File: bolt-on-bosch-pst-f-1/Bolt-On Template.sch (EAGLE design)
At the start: 10 parts

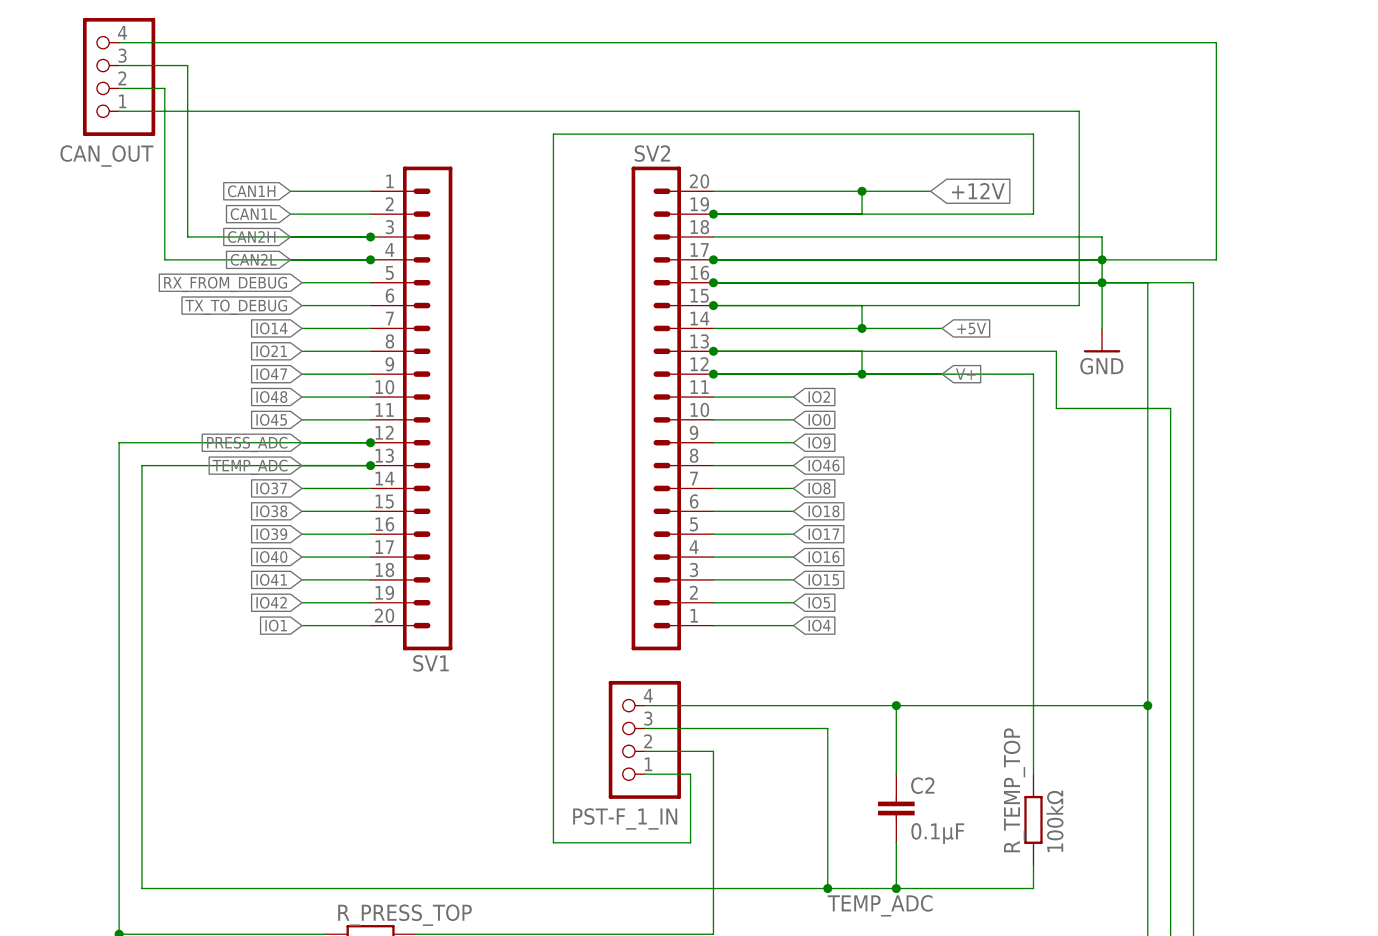
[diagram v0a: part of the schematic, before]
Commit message: designed circuit board for bosch sensor
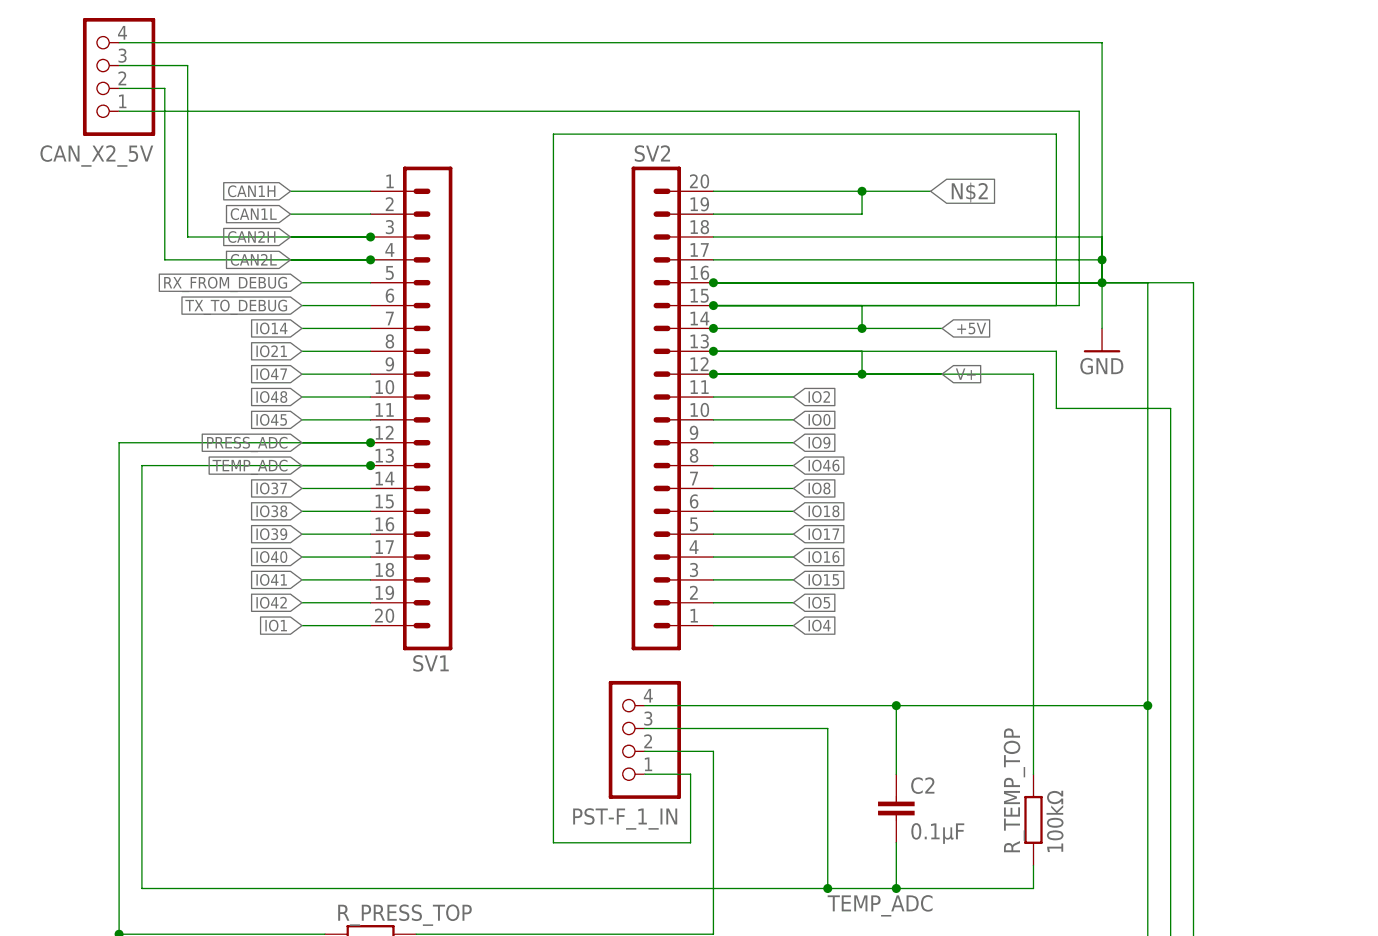
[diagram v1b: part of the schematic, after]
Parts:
- removed CAN_OUT: (no value), JST PH Library:S4B-PH-SM4-TB
- added CAN_X2_5V: (no value), JST PH Library:S4B-PH-K-S
- PST-F_1_IN: device JST PH Library:S4B-PH-SM4-TB -> JST PH Library:S4B-PH-K-S
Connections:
- removed net +12V: PST-F_1_IN.1, SV2.19, SV2.20
- new net N$2: SV2.19, SV2.20
- net +5V: now also CAN_X2_5V.1, PST-F_1_IN.1; no longer CAN_OUT.1
- net CAN2H: now also CAN_X2_5V.3; no longer CAN_OUT.3
- net CAN2L: now also CAN_X2_5V.2; no longer CAN_OUT.2
- net GND: now also CAN_X2_5V.4; no longer CAN_OUT.4
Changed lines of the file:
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@@
 <part name="R_PRESS_BOT" library="rcl" library_urn="urn:adsk.eagle:library:334" deviceset="R-EU_" device="R0805" package3d_urn="urn:adsk.eagle:package:23553/2" value="10kΩ"/>
 <part name="C2" library="rcl" library_urn="urn:adsk.eagle:library:334" deviceset="C-EU" device="C0805" package3d_urn="urn:adsk.eagle:package:23617/2" value="0.1µF"/>
-<part name="CAN_OUT" library="JST PH Library" deviceset="S4B-PH-*" device="SM4-TB"/>
-<part name="PST-F_1_IN" library="JST PH Library" deviceset="S4B-PH-*" device="SM4-TB"/>
+<part name="CAN_X2_5V" library="JST PH Library" deviceset="S4B-PH-*" device="K-S"/>
+<part name="PST-F_1_IN" library="JST PH Library" deviceset="S4B-PH-*" device="K-S"/>
 </parts>
 <sheets>
@@
 <attribute name="VALUE" x="235.204" y="81.661" size="1.778" layer="96"/>
 </instance>
-<instance part="CAN_OUT" gate="G$1" x="147.32" y="165.1" smashed="yes" rot="R180">
+<instance part="CAN_X2_5V" gate="G$1" x="147.32" y="165.1" smashed="yes" rot="R180">
 <attribute name="NAME" x="151.13" y="158.75" size="1.778" layer="95" rot="R180"/>
 <attribute name="VALUE" x="151.13" y="175.26" size="1.778" layer="96" rot="R180"/>
@@
 <wire x1="256.54" y1="143.51" x2="256.54" y2="146.05" width="0.1524" layer="91"/>
 <junction x="256.54" y="143.51"/>
-<wire x1="205.74" y1="96.52" x2="233.68" y2="96.52" width="0.1524" layer="91"/>
 <wire x1="233.68" y1="96.52" x2="261.62" y2="96.52" width="0.1524" layer="91"/>
 <wire x1="261.62" y1="96.52" x2="261.62" y2="143.51" width="0.1524" layer="91"/>
@@
 <junction x="213.36" y="143.51"/>
 <wire x1="233.68" y1="88.9" x2="233.68" y2="96.52" width="0.1524" layer="91"/>
-<junction x="233.68" y="96.52"/>
 <wire x1="266.7" y1="143.51" x2="213.36" y2="143.51" width="0.1524" layer="91"/>
 <wire x1="261.62" y1="66.04" x2="261.62" y2="96.52" width="0.1524" layer="91"/>
@@
 <pinref part="C1" gate="G$1" pin="1"/>
 <pinref part="C2" gate="G$1" pin="1"/>
-<pinref part="CAN_OUT" gate="G$1" pin="4"/>
-<wire x1="147.32" y1="170.18" x2="269.24" y2="170.18" width="0.1524" layer="91"/>
-<wire x1="269.24" y1="170.18" x2="269.24" y2="146.05" width="0.1524" layer="91"/>
-<wire x1="269.24" y1="146.05" x2="213.36" y2="146.05" width="0.1524" layer="91"/>
-<junction x="213.36" y="146.05"/>
+<wire x1="256.54" y1="170.18" x2="256.54" y2="143.51" width="0.1524" layer="91"/>
+<pinref part="CAN_X2_5V" gate="G$1" pin="4"/>
+<wire x1="256.54" y1="170.18" x2="147.32" y2="170.18" width="0.1524" layer="91"/>
 <pinref part="PST-F_1_IN" gate="G$1" pin="4"/>
+<wire x1="233.68" y1="96.52" x2="205.74" y2="96.52" width="0.1524" layer="91"/>
+<junction x="233.68" y="96.52"/>
 </segment>
 </net>
@@
 </segment>
 </net>
-<net name="+12V" class="0">
-<segment>
-<pinref part="SV2" gate="1" pin="20"/>
-<wire x1="213.36" y1="153.67" x2="229.87" y2="153.67" width="0.1524" layer="91"/>
-<label x="237.49" y="153.67" size="1.778" layer="95" xref="yes"/>
-<pinref part="SV2" gate="1" pin="19"/>
-<wire x1="229.87" y1="153.67" x2="237.49" y2="153.67" width="0.1524" layer="91"/>
-<wire x1="213.36" y1="151.13" x2="229.87" y2="151.13" width="0.1524" layer="91"/>
-<wire x1="229.87" y1="151.13" x2="229.87" y2="153.67" width="0.1524" layer="91"/>
-<junction x="229.87" y="153.67"/>
-<wire x1="205.74" y1="88.9" x2="210.82" y2="88.9" width="0.1524" layer="91"/>
-<wire x1="210.82" y1="88.9" x2="210.82" y2="81.28" width="0.1524" layer="91"/>
-<wire x1="210.82" y1="81.28" x2="195.58" y2="81.28" width="0.1524" layer="91"/>
-<wire x1="195.58" y1="81.28" x2="195.58" y2="160.02" width="0.1524" layer="91"/>
-<wire x1="195.58" y1="160.02" x2="248.92" y2="160.02" width="0.1524" layer="91"/>
-<wire x1="248.92" y1="160.02" x2="248.92" y2="151.13" width="0.1524" layer="91"/>
-<wire x1="248.92" y1="151.13" x2="213.36" y2="151.13" width="0.1524" layer="91"/>
-<junction x="213.36" y="151.13"/>
-<pinref part="PST-F_1_IN" gate="G$1" pin="1"/>
-</segment>
-</net>
 <net name="CAN1H" class="0">
 <segment>
@@
 <wire x1="175.26" y1="148.59" x2="166.37" y2="148.59" width="0.1524" layer="91"/>
 <label x="166.37" y="148.59" size="1.27" layer="95" rot="R180" xref="yes"/>
-<pinref part="CAN_OUT" gate="G$1" pin="3"/>
-<wire x1="147.32" y1="167.64" x2="154.94" y2="167.64" width="0.1524" layer="91"/>
 <wire x1="154.94" y1="167.64" x2="154.94" y2="148.59" width="0.1524" layer="91"/>
 <wire x1="154.94" y1="148.59" x2="175.26" y2="148.59" width="0.1524" layer="91"/>
 <junction x="175.26" y="148.59"/>
+<pinref part="CAN_X2_5V" gate="G$1" pin="3"/>
+<wire x1="154.94" y1="167.64" x2="147.32" y2="167.64" width="0.1524" layer="91"/>
 </segment>
 </net>
@@
 <wire x1="175.26" y1="146.05" x2="166.37" y2="146.05" width="0.1524" layer="91"/>
 <label x="166.37" y="146.05" size="1.27" layer="95" rot="R180" xref="yes"/>
-<pinref part="CAN_OUT" gate="G$1" pin="2"/>
-<wire x1="147.32" y1="165.1" x2="152.4" y2="165.1" width="0.1524" layer="91"/>
 <wire x1="152.4" y1="165.1" x2="152.4" y2="146.05" width="0.1524" layer="91"/>
 <wire x1="152.4" y1="146.05" x2="175.26" y2="146.05" width="0.1524" layer="91"/>
 <junction x="175.26" y="146.05"/>
+<pinref part="CAN_X2_5V" gate="G$1" pin="2"/>
+<wire x1="152.4" y1="165.1" x2="147.32" y2="165.1" width="0.1524" layer="91"/>
 </segment>
 </net>
@@
 <wire x1="175.26" y1="105.41" x2="167.64" y2="105.41" width="0.1524" layer="91"/>
 <label x="167.64" y="105.41" size="1.27" layer="95" rot="R180" xref="yes"/>
-</segment>
-</net>
-<net name="+5V" class="0">
-<segment>
-<wire x1="229.87" y1="138.43" x2="238.76" y2="138.43" width="0.1524" layer="91"/>
-<pinref part="SV2" gate="1" pin="15"/>
-<wire x1="213.36" y1="140.97" x2="229.87" y2="140.97" width="0.1524" layer="91"/>
-<wire x1="229.87" y1="140.97" x2="229.87" y2="138.43" width="0.1524" layer="91"/>
-<junction x="229.87" y="138.43"/>
-<pinref part="SV2" gate="1" pin="14"/>
-<wire x1="213.36" y1="138.43" x2="229.87" y2="138.43" width="0.1524" layer="91"/>
-<label x="238.76" y="138.43" size="1.27" layer="95" xref="yes"/>
-<wire x1="147.32" y1="162.56" x2="254" y2="162.56" width="0.1524" layer="91"/>
-<wire x1="254" y1="162.56" x2="254" y2="140.97" width="0.1524" layer="91"/>
-<wire x1="254" y1="140.97" x2="213.36" y2="140.97" width="0.1524" layer="91"/>
-<junction x="213.36" y="140.97"/>
-<pinref part="CAN_OUT" gate="G$1" pin="1"/>
 </segment>
 </net>
@@
 <wire x1="149.86" y1="123.19" x2="175.26" y2="123.19" width="0.1524" layer="91"/>
 <junction x="175.26" y="123.19"/>
-<wire x1="205.74" y1="93.98" x2="226.06" y2="93.98" width="0.1524" layer="91"/>
 <wire x1="226.06" y1="93.98" x2="226.06" y2="76.2" width="0.1524" layer="91"/>
 <pinref part="R_TEMP_TOP" gate="G$1" pin="1"/>
@@
 <pinref part="C2" gate="G$1" pin="2"/>
 <pinref part="PST-F_1_IN" gate="G$1" pin="3"/>
+<wire x1="226.06" y1="93.98" x2="205.74" y2="93.98" width="0.1524" layer="91"/>
 </segment>
 </net>
 <net name="N$1" class="0">
 <segment>
-<wire x1="205.74" y1="91.44" x2="213.36" y2="91.44" width="0.1524" layer="91"/>
 <wire x1="213.36" y1="91.44" x2="213.36" y2="71.12" width="0.1524" layer="91"/>
 <wire x1="213.36" y1="71.12" x2="180.34" y2="71.12" width="0.1524" layer="91"/>
 <pinref part="R_PRESS_TOP" gate="G$1" pin="2"/>
 <pinref part="PST-F_1_IN" gate="G$1" pin="2"/>
+<wire x1="213.36" y1="91.44" x2="205.74" y2="91.44" width="0.1524" layer="91"/>
 </segment>
 </net>
@@
 </segment>
 </net>
+<net name="N$2" class="0">
+<segment>
+<pinref part="SV2" gate="1" pin="20"/>
+<wire x1="213.36" y1="153.67" x2="229.87" y2="153.67" width="0.1524" layer="91"/>
+<wire x1="229.87" y1="153.67" x2="237.49" y2="153.67" width="0.1524" layer="91"/>
+<junction x="229.87" y="153.67"/>
+<wire x1="229.87" y1="151.13" x2="229.87" y2="153.67" width="0.1524" layer="91"/>
+<pinref part="SV2" gate="1" pin="19"/>
+<wire x1="213.36" y1="151.13" x2="229.87" y2="151.13" width="0.1524" layer="91"/>
+<label x="237.49" y="153.67" size="1.778" layer="95" xref="yes"/>
+</segment>
+</net>
+<net name="+5V" class="0">
+<segment>
+<wire x1="210.82" y1="88.9" x2="210.82" y2="81.28" width="0.1524" layer="91"/>
+<wire x1="210.82" y1="81.28" x2="195.58" y2="81.28" width="0.1524" layer="91"/>
+<wire x1="195.58" y1="81.28" x2="195.58" y2="160.02" width="0.1524" layer="91"/>
+<wire x1="195.58" y1="160.02" x2="251.46" y2="160.02" width="0.1524" layer="91"/>
+<wire x1="229.87" y1="138.43" x2="238.76" y2="138.43" width="0.1524" layer="91"/>
+<pinref part="SV2" gate="1" pin="15"/>
+<wire x1="213.36" y1="140.97" x2="229.87" y2="140.97" width="0.1524" layer="91"/>
+<wire x1="229.87" y1="140.97" x2="229.87" y2="138.43" width="0.1524" layer="91"/>
+<junction x="229.87" y="138.43"/>
+<pinref part="SV2" gate="1" pin="14"/>
+<wire x1="213.36" y1="138.43" x2="229.87" y2="138.43" width="0.1524" layer="91"/>
+<label x="238.76" y="138.43" size="1.27" layer="95" xref="yes"/>
+<wire x1="254" y1="162.56" x2="254" y2="140.97" width="0.1524" layer="91"/>
+<wire x1="254" y1="140.97" x2="213.36" y2="140.97" width="0.1524" layer="91"/>
+<junction x="213.36" y="138.43"/>
+<wire x1="251.46" y1="160.02" x2="251.46" y2="140.97" width="0.1524" layer="91"/>
+<wire x1="251.46" y1="140.97" x2="213.36" y2="140.97" width="0.1524" layer="91"/>
+<junction x="213.36" y="140.97"/>
+<pinref part="CAN_X2_5V" gate="G$1" pin="1"/>
+<wire x1="254" y1="162.56" x2="147.32" y2="162.56" width="0.1524" layer="91"/>
+<pinref part="PST-F_1_IN" gate="G$1" pin="1"/>
+<wire x1="210.82" y1="88.9" x2="205.74" y2="88.9" width="0.1524" layer="91"/>
+</segment>
+</net>
 </nets>
 </sheet>
 </sheets>
-<errors>
-</errors>
 </schematic>
 </drawing>

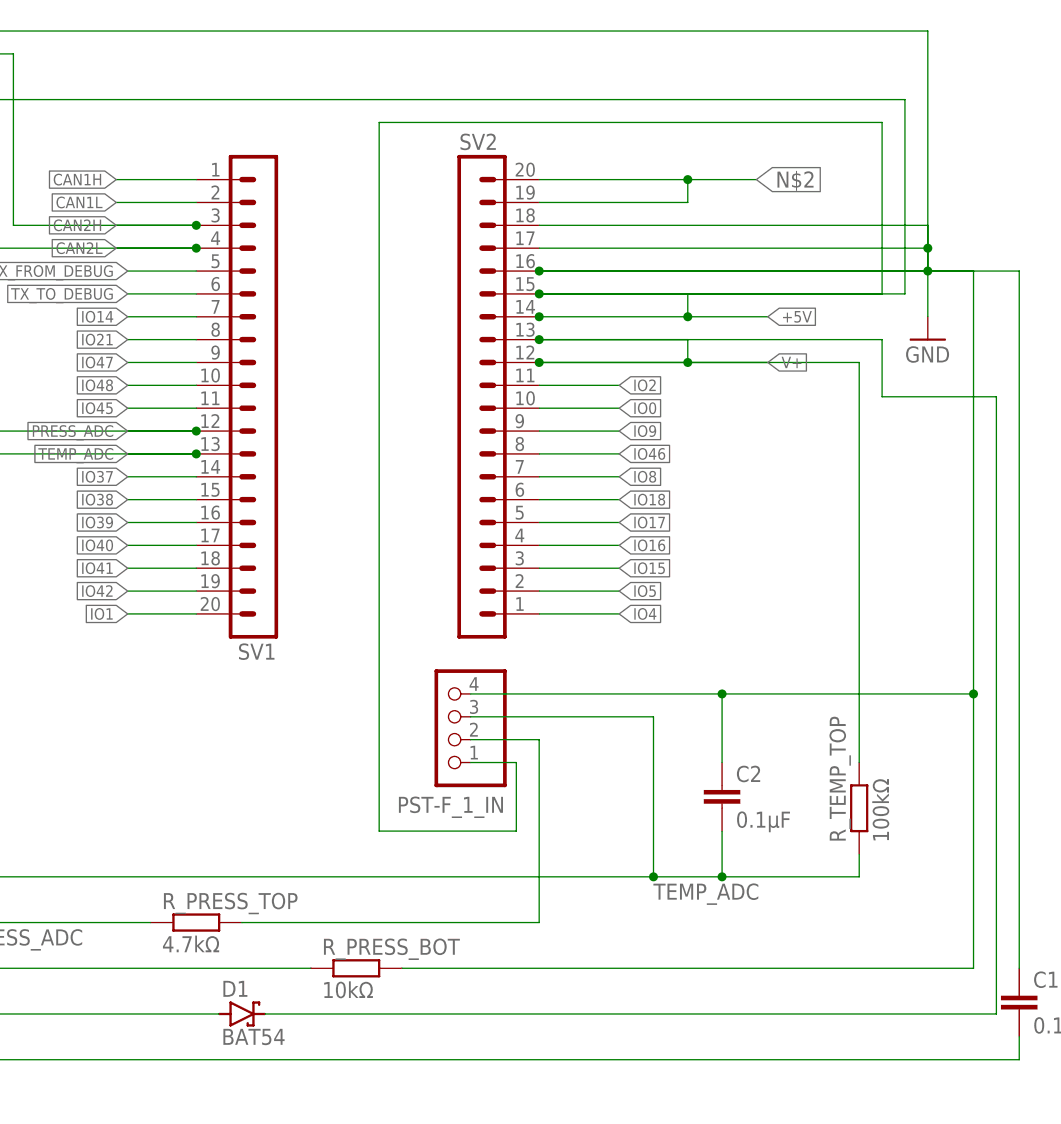
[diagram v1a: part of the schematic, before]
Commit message: added readme for daughter board design
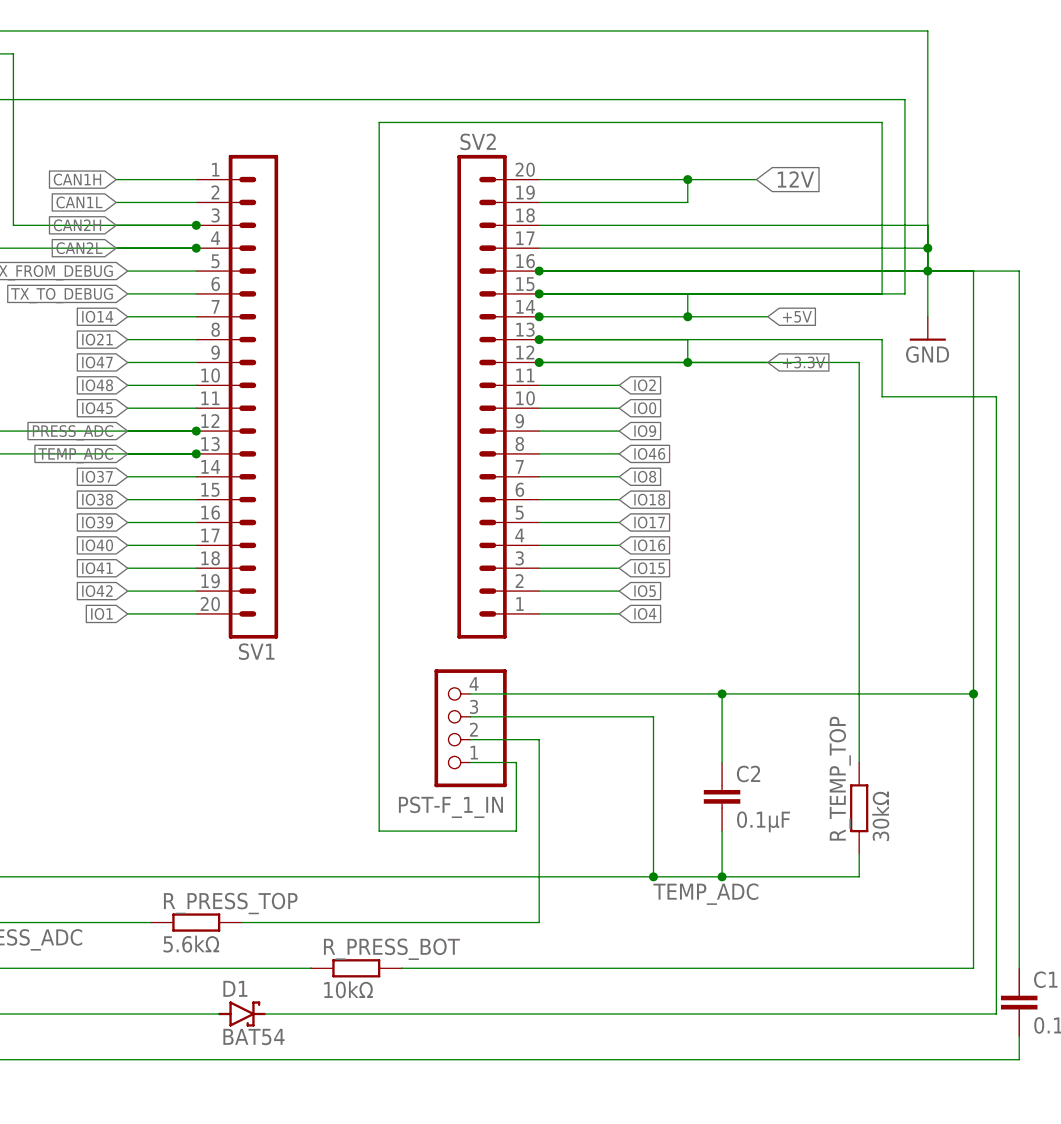
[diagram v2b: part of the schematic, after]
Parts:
- R_PRESS_TOP: value 4.7kΩ -> 5.6kΩ
- R_TEMP_TOP: value 100kΩ -> 30kΩ
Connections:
- net N$2 renamed 12V
- net V+ renamed +3.3V
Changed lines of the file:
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@@
 <part name="GND5" library="supply1" deviceset="GND" device=""/>
 <part name="D1" library="diode" library_urn="urn:adsk.eagle:library:210" deviceset="BAT54" device="" package3d_urn="urn:adsk.eagle:package:43389/2"/>
-<part name="R_TEMP_TOP" library="rcl" library_urn="urn:adsk.eagle:library:334" deviceset="R-EU_" device="R0805" package3d_urn="urn:adsk.eagle:package:23553/2" value="100kΩ"/>
+<part name="R_TEMP_TOP" library="rcl" library_urn="urn:adsk.eagle:library:334" deviceset="R-EU_" device="R0805" package3d_urn="urn:adsk.eagle:package:23553/2" value="30kΩ"/>
 <part name="C1" library="rcl" library_urn="urn:adsk.eagle:library:334" deviceset="C-EU" device="C0805" package3d_urn="urn:adsk.eagle:package:23617/2" value="0.1µF"/>
-<part name="R_PRESS_TOP" library="rcl" library_urn="urn:adsk.eagle:library:334" deviceset="R-EU_" device="R0805" package3d_urn="urn:adsk.eagle:package:23553/2" value="4.7kΩ"/>
+<part name="R_PRESS_TOP" library="rcl" library_urn="urn:adsk.eagle:library:334" deviceset="R-EU_" device="R0805" package3d_urn="urn:adsk.eagle:package:23553/2" value="5.6kΩ"/>
 <part name="R_PRESS_BOT" library="rcl" library_urn="urn:adsk.eagle:library:334" deviceset="R-EU_" device="R0805" package3d_urn="urn:adsk.eagle:package:23553/2" value="10kΩ"/>
 <part name="C2" library="rcl" library_urn="urn:adsk.eagle:library:334" deviceset="C-EU" device="C0805" package3d_urn="urn:adsk.eagle:package:23617/2" value="0.1µF"/>
@@
 </segment>
 </net>
-<net name="V+" class="0">
+<net name="+3.3V" class="0">
 <segment>
 <pinref part="SV2" gate="1" pin="12"/>
@@
 </segment>
 </net>
-<net name="N$2" class="0">
+<net name="12V" class="0">
 <segment>
 <pinref part="SV2" gate="1" pin="20"/>
